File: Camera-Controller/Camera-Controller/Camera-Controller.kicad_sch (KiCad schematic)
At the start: 39 parts, among them J1 RBUS, U1 ESP32-S3, Y1 R940000171

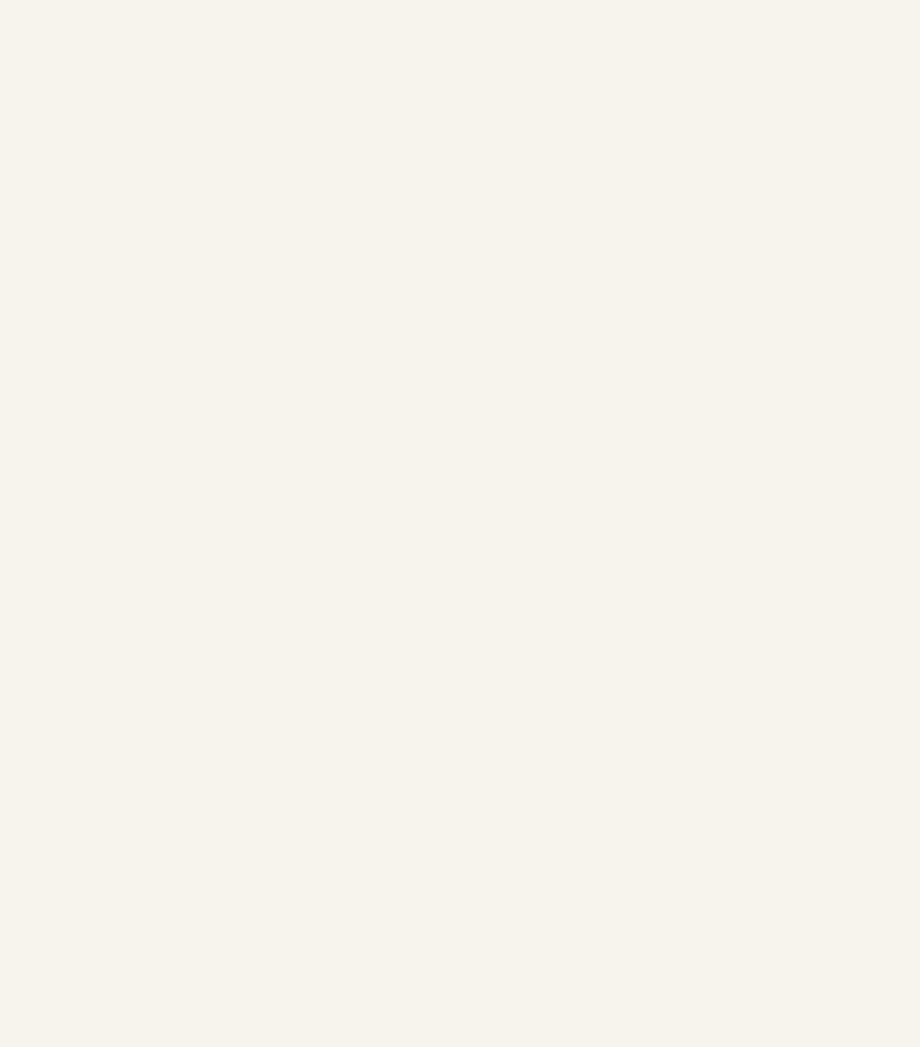
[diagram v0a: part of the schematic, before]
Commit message: CM5 schematic drawn [KiCad]
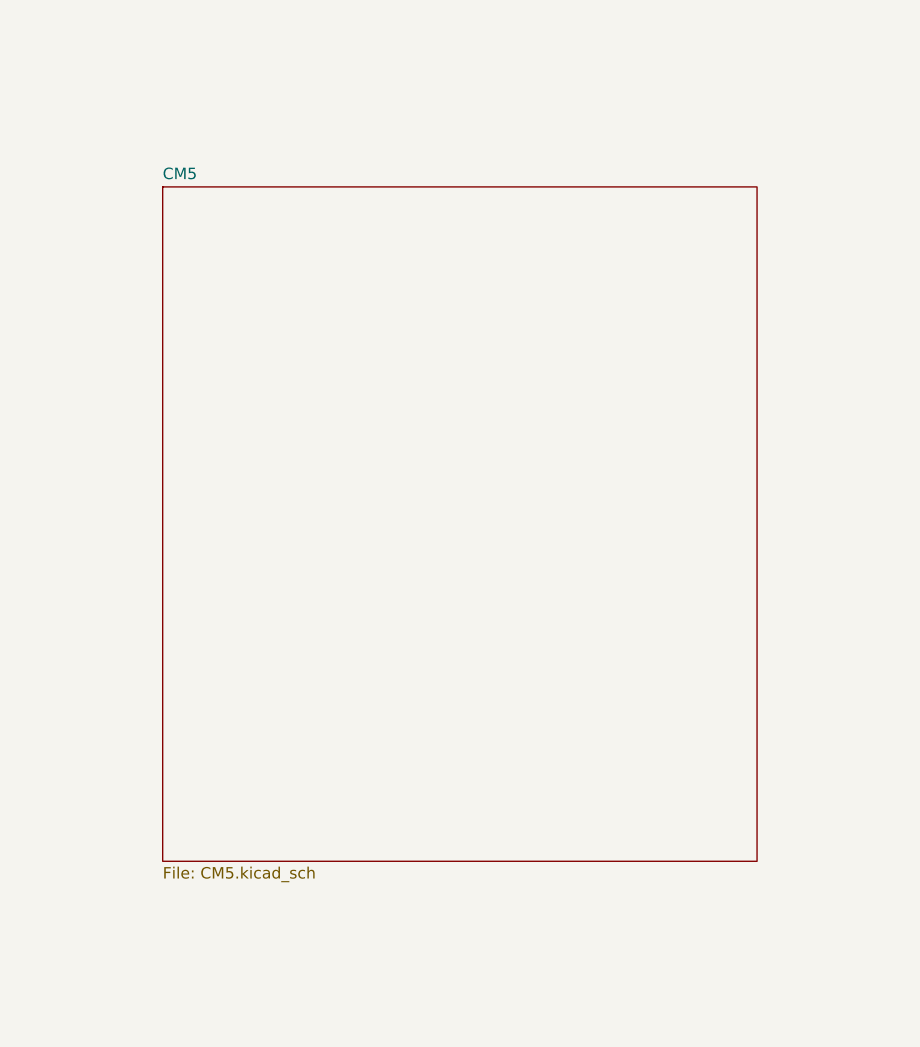
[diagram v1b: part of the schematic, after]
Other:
- added sheet CM5 (CM5.kicad_sch)
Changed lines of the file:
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@@
 		)
 		(instances
-			(project "RicardoTemplate"
+			(project "Camera-Controller"
 				(path "/7db990e4-92e1-4f99-b4d2-435bbec1ba83"
 					(page "3")
@@
 		)
 		(instances
-			(project "RicardoTemplate"
+			(project "Camera-Controller"
 				(path "/7db990e4-92e1-4f99-b4d2-435bbec1ba83"
 					(page "2")
@@
 		)
 		(instances
-			(project "RicardoTemplate"
+			(project "Camera-Controller"
 				(path "/7db990e4-92e1-4f99-b4d2-435bbec1ba83"
 					(page "4")
 				)
 			)
+		)
+	)
+	(sheet
+		(at 194.31 72.39)
+		(size 66.04 74.93)
+		(exclude_from_sim no)
+		(in_bom yes)
+		(on_board yes)
+		(dnp no)
+		(fields_autoplaced yes)
+		(stroke
+			(width 0.1524)
+			(type solid)
+		)
+		(fill
+			(color 0 0 0 0.0000)
+		)
+		(property "Sheetname" "CM5"
+			(at 194.31 71.6784 0)
+			(effects
+				(font
+					(size 1.27 1.27)
+				)
+				(justify left bottom)
+			)
+		)
+		(property "Sheetfile" "CM5.kicad_sch"
+			(at 194.31 147.9046 0)
+			(effects
+				(font
+					(size 1.27 1.27)
+				)
+				(justify left top)
+			)
+		)
+		(instances
+			(project "Camera-Controller"
+				(path "/7db990e4-92e1-4f99-b4d2-435bbec1ba83"
+					(page "5")
+				)
+			)
